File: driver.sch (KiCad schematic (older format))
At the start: 50 parts

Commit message: 5V raus
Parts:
- removed C?: 10u0, symbol Device:C
- removed C?: 10n0, symbol Device:C
- removed C?: 220u, symbol Device:C
- removed D?: B340, Diode_SMD:D_SMC, symbol Diode:B340
- removed L?: 15u0, symbol Device:L
- removed R?: 10k0, symbol Device:R
- removed R?: 3k24, symbol Device:R
- removed U?: TPS5430DDA, Package_SO:TI_SO-PowerPAD-8_ThermalVias, symbol Regulator_Switching:TPS5430DDA
- R?: value 3k24 -> 5k8
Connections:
- net labels removed: +5V
- wire segments 217 -> 190
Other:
- moved on the sheet: C?, D?, L?, R?, U?

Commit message: Power Supply geändert
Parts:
- removed C? (x2): 10u0, symbol Device:C
- removed C? (x2): 10n0, symbol Device:C
- removed C?: 220u, symbol Device:C
- removed C?: 10u0 / 75V, symbol Device:C
- removed C?: C, symbol Device:C
- removed C?: 10u0 / 16V, symbol Device:C
- removed C?: 100u, symbol Device:CP
- removed D?: B340, Diode_SMD:D_SMC, symbol Diode:B340
- removed L?: 15u0, symbol Device:L
- removed L?: L, symbol Device:L
- removed R? (x2): 10k0, symbol Device:R
- removed R?: 5k8, symbol Device:R
- removed R?: 402k, symbol Device:R
- removed R?: 2k00, symbol Device:R
- removed U?: TPS5430DDA, Package_SO:TI_SO-PowerPAD-8_ThermalVias, symbol Regulator_Switching:TPS5430DDA
- removed U?: LM5161, Package_SON:Texas_S-PVSON-N10_ThermalVias, symbol gsvesc:LM5161
- added C16: 10u/75V, symbol Device:C
- added C17, C19: 100n, symbol Device:C
- added C20, C23, C31: 10n0, symbol Device:C
- added C26: 22uF, symbol Device:C
- added C28: 10u0/25V, symbol Device:C
- added C33, C34: 100u, Capacitor_Tantalum_SMD:CP_EIA-3528-21_Kemet-B, symbol Device:CP
- added D4, D5: B360, Diode_SMD:D_SMC, symbol Diode:B360
- added L1: 470u, symbol Device:L
- added L2: 15u0, symbol Device:L
- added R12, R15: 680k, Resistor_SMD:R_0805_2012Metric, symbol Device:R
- added R16, R27: 10k0, Resistor_SMD:R_0805_2012Metric, symbol Device:R
- added R23: 2k70, Resistor_SMD:R_0805_2012Metric, symbol Device:R
- added R24: 1R00, Resistor_SMD:R_0805_2012Metric, symbol Device:R
- added R34: 5k90, Resistor_SMD:R_0805_2012Metric, symbol Device:R
- added U10: LM5008MM, Package_SO:MSOP-8_3x3mm_P0.65mm, symbol Regulator_Switching:LM5008MM
- added U14: TPS5430DDA, Package_SO:TI_SO-PowerPAD-8_ThermalVias, symbol Regulator_Switching:TPS5430DDA
- C15, C22, C29: renamed from C?; value 10u -> 10u0/25V; footprint (none) -> Capacitor_SMD:C_0805_2012Metric
- C18, C25, C30: renamed from C?; value C -> 100n; footprint (none) -> Capacitor_SMD:C_0805_2012Metric
- C21, C27, C32: renamed from C?; footprint (none) -> Capacitor_SMD:C_0805_2012Metric
- R13, R14, R17, R18, R19, R20, R21, R22: renamed from R?; footprint (none) -> Resistor_SMD:R_0805_2012Metric
- gave numbers to parts that had none: 6
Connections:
- net labels added: EXT_OFF
- wire segments 190 -> 191

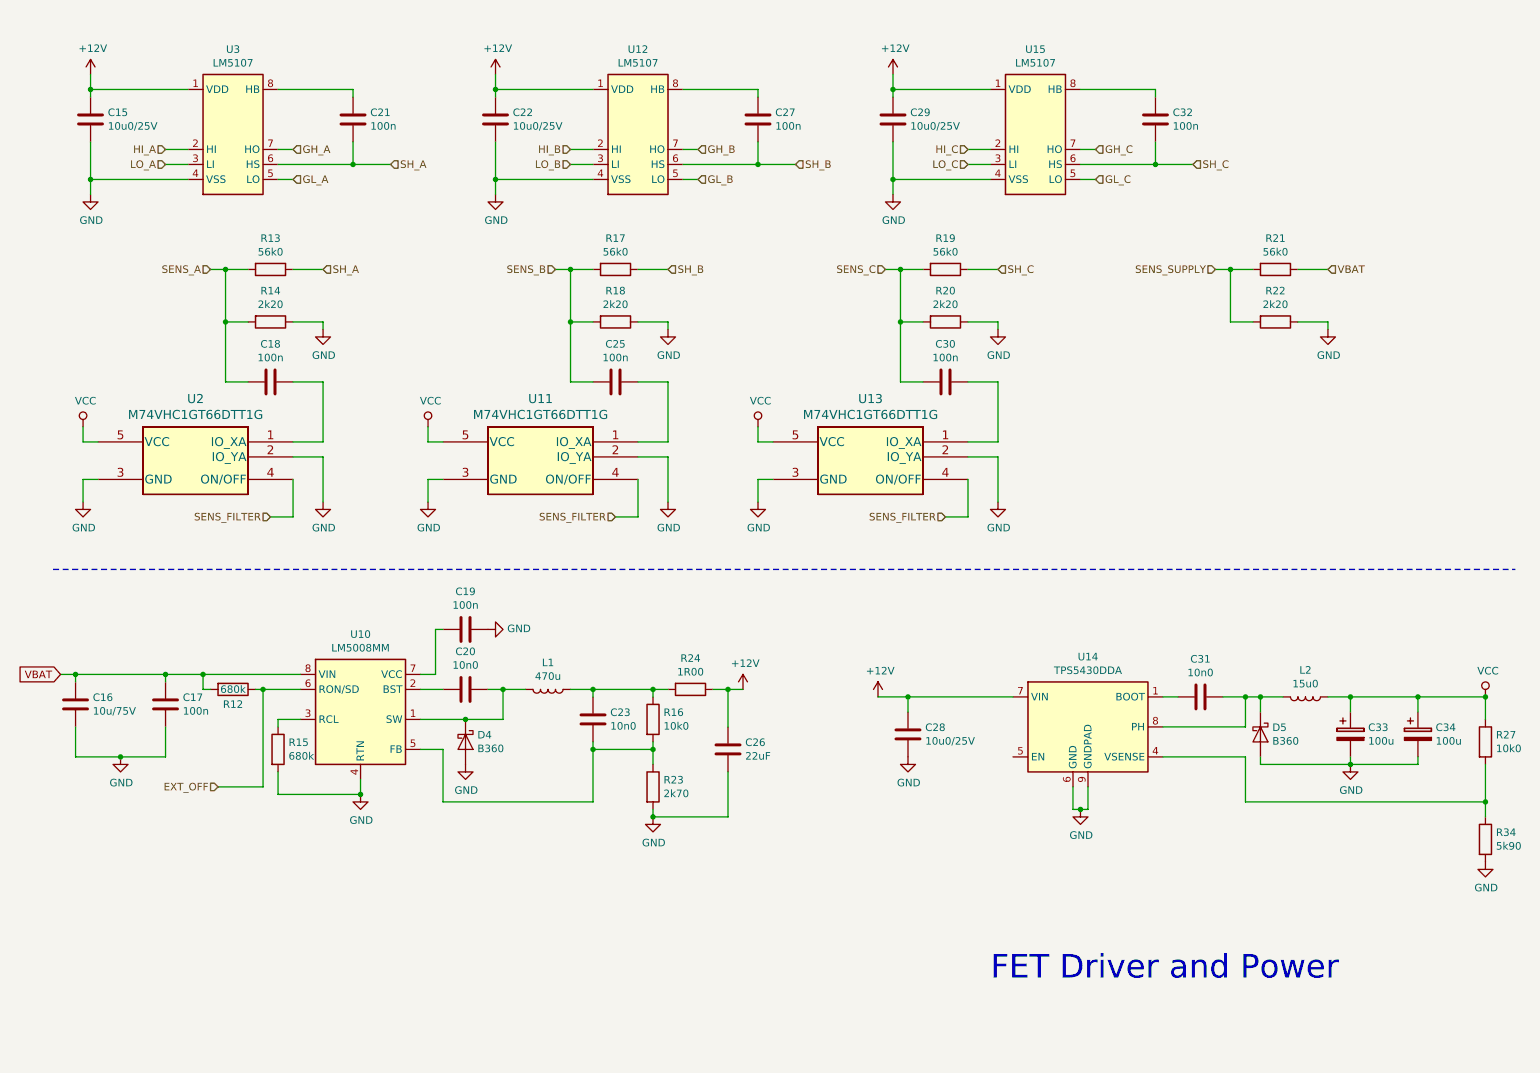
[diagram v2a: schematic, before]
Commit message: Powersupply geändert
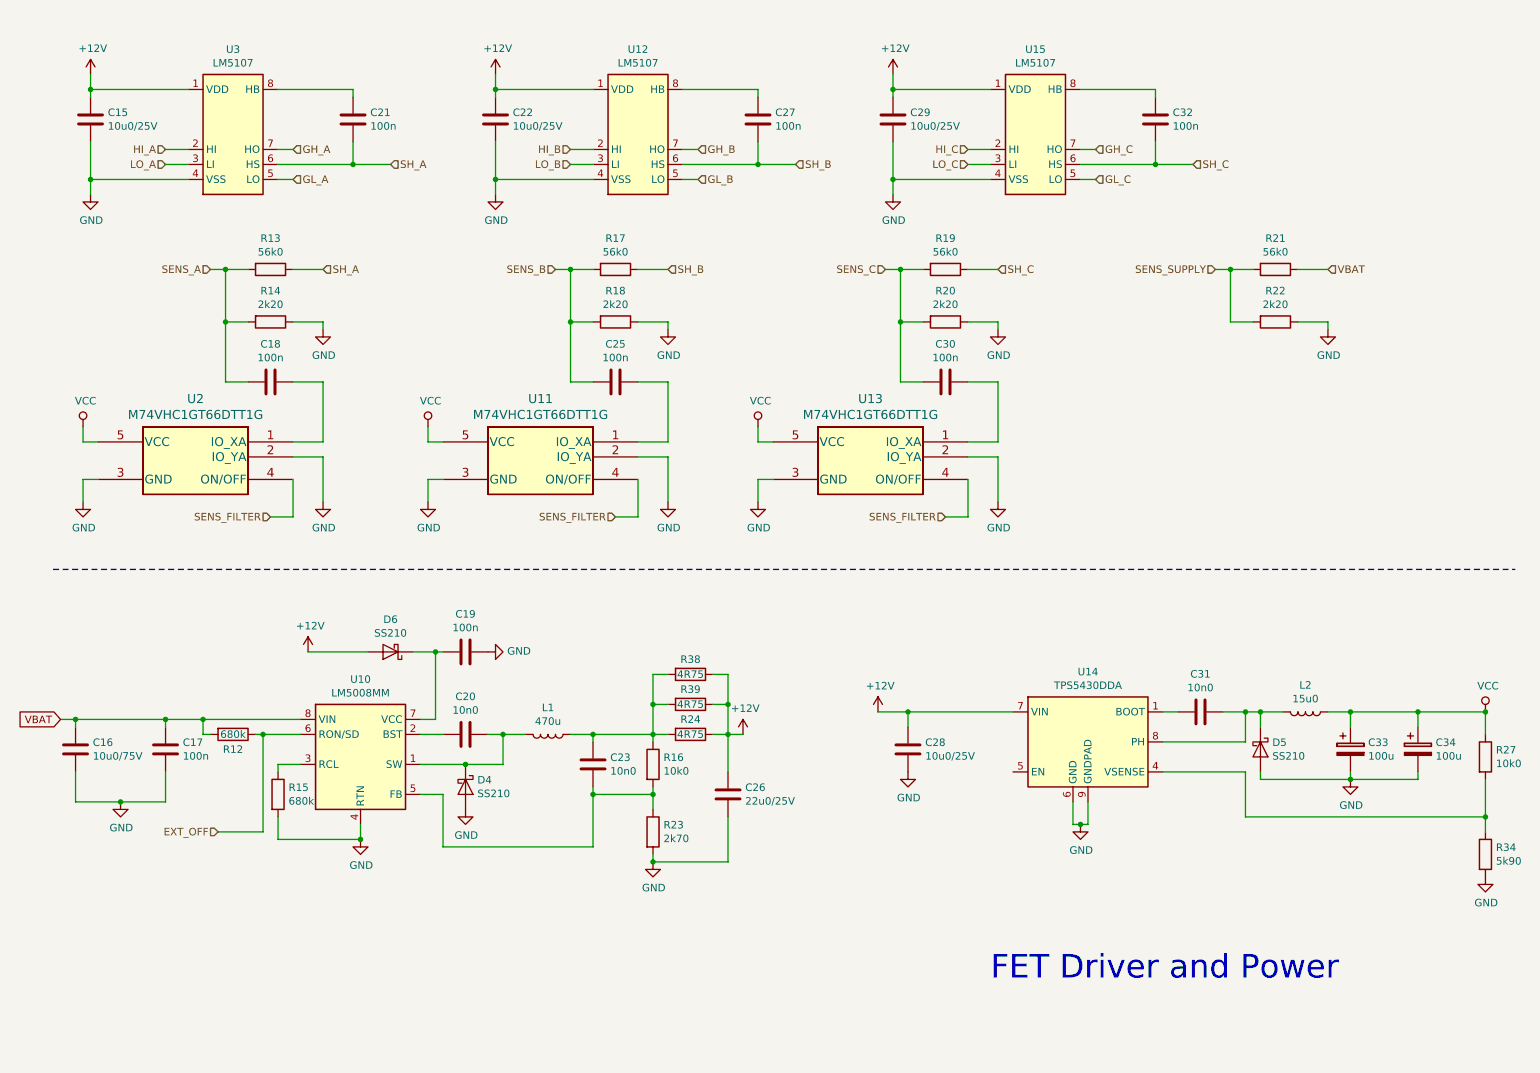
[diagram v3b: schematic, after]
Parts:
- added D6: SS210, Diode_SMD:D_SMA, symbol Device:D_Schottky
- added R38, R39: 4R75, Resistor_SMD:R_0805_2012Metric, symbol Device:R
- C16: value 10u/75V -> 10u0/75V; footprint (none) -> Capacitor_SMD:C_1210_3225Metric
- C17, C19, C20, C23, C28, C31: footprint (none) -> Capacitor_SMD:C_0805_2012Metric
- C26: value 22uF -> 22u0/25V; footprint (none) -> Capacitor_SMD:C_0805_2012Metric
- D4, D5: value B360 -> SS210; footprint Diode_SMD:D_SMC -> Diode_SMD:D_SMA; LCSC (none) -> C14996
- L1: footprint (none) -> Inductor_SMD:L_12x12mm_H6mm; LCSC (none) -> C169382; Partnumber (none) -> SWRB1207S-471MT
- L2: footprint (none) -> Inductor_SMD:L_12x12mm_H6mm; LCSC (none) -> C169384; Partnumber (none) -> SWRB1205S-150MT
- R24: value 1R00 -> 4R75
- U11, U13, U2: footprint TSOP-5 -> gsvesc:M74VHC1GT66DTT1G
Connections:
- net +12V: now also D6.2 (A), R38.1, R39.1
- net at C19.1, U10.7 (VCC): now also D6.1 (K)
- net at C23.1, L1.1, R16.1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: now also R38.2, R39.2
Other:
- moved on the sheet: C16, C17, C19, C20, C23, C26, C28, C31, C33, C34, D4, D5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

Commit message: V4 pre
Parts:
- added D7: B5819W, Diode_SMD:D_SOD-123, symbol Device:D_Schottky
- D6: value SS210 -> B5819W; footprint Diode_SMD:D_SMA -> Diode_SMD:D_SOD-123; LCSC C14996 -> C8598
- L2: footprint Inductor_SMD:L_12x12mm_H6mm -> Inductor_SMD:L_7.3x7.3_H4.5; LCSC C169384 -> C132136
- R14, R18, R20, R22: value 2k20 -> 2k70
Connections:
- net +12V: now also D7.1 (K)
- new net +5V: D7.2 (A)
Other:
- note added: "USB powered"
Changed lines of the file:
@@
 P 9050 2550
 F 0 "R22" V 8843 2550 50  0000 C CNN
-F 1 "2k20" V 8934 2550 50  0000 C CNN
+F 1 "2k70" V 8934 2550 50  0000 C CNN
 F 2 "Resistor_SMD:R_0805_2012Metric" V 8980 2550 50  0001 C CNN
 F 3 "~" H 9050 2550 50  0001 C CNN
@@
 P 6850 2550
 F 0 "R20" V 6643 2550 50  0000 C CNN
-F 1 "2k20" V 6734 2550 50  0000 C CNN
+F 1 "2k70" V 6734 2550 50  0000 C CNN
 F 2 "Resistor_SMD:R_0805_2012Metric" V 6780 2550 50  0001 C CNN
 F 3 "~" H 6850 2550 50  0001 C CNN
@@
 P 4650 2550
 F 0 "R18" V 4443 2550 50  0000 C CNN
-F 1 "2k20" V 4534 2550 50  0000 C CNN
+F 1 "2k70" V 4534 2550 50  0000 C CNN
 F 2 "Resistor_SMD:R_0805_2012Metric" V 4580 2550 50  0001 C CNN
 F 3 "~" H 4650 2550 50  0001 C CNN
@@
 P 2350 2550
 F 0 "R14" V 2143 2550 50  0000 C CNN
-F 1 "2k20" V 2234 2550 50  0000 C CNN
+F 1 "2k70" V 2234 2550 50  0000 C CNN
 F 2 "Resistor_SMD:R_0805_2012Metric" V 2280 2550 50  0001 C CNN
 F 3 "~" H 2350 2550 50  0001 C CNN
@@
 Wire Wire Line
 	4500 5700 4500 6050
-Wire Wire Line
-	7300 5150 6600 5150
 $Comp
 L power:+12V #PWR0147
@@
 F 0 "L2" V 9072 5150 50  0000 C CNN
 F 1 "15u0" V 9163 5150 50  0000 C CNN
-F 2 "Inductor_SMD:L_12x12mm_H6mm" H 9250 5150 50  0001 C CNN
+F 2 "Inductor_SMD:L_7.3x7.3_H4.5" H 9250 5150 50  0001 C CNN
 F 3 "~" H 9250 5150 50  0001 C CNN
 F 4 "SWRB1205S-150MT" V 9250 5150 50  0001 C CNN "Partnumber"
-F 5 "C169384" V 9250 5150 50  0001 C CNN "LCSC"
+F 5 "C132136" V 9250 5150 50  0001 C CNN "LCSC"
 	1    9250 5150
 	0    1    1    0
@@
 P 3150 4750
 F 0 "D6" H 3150 4534 50  0000 C CNN
-F 1 "SS210" H 3150 4625 50  0000 C CNN
-F 2 "Diode_SMD:D_SMA" H 3150 4750 50  0001 C CNN
+F 1 "B5819W" H 3150 4625 50  0000 C CNN
+F 2 "Diode_SMD:D_SOD-123" H 3150 4750 50  0001 C CNN
 F 3 "~" H 3150 4750 50  0001 C CNN
-F 4 "C14996" H 3150 4750 50  0001 C CNN "LCSC"
+F 4 "C8598" H 3150 4750 50  0001 C CNN "LCSC"
 	1    3150 4750
 	-1   0    0    1
@@
 	0    1    1    0
 $EndComp
+$Comp
+L Device:D_Schottky D7
+U 1 1 5E97305F
+P 7050 4900
+F 0 "D7" V 7100 4800 50  0000 C CNN
+F 1 "B5819W" V 7200 4700 50  0000 C CNN
+F 2 "Diode_SMD:D_SOD-123" H 7050 4900 50  0001 C CNN
+F 3 "~" H 7050 4900 50  0001 C CNN
+F 4 "C8598" H 7050 4900 50  0001 C CNN "LCSC"
+	1    7050 4900
+	0    -1   -1   0
+$EndComp
+Wire Wire Line
+	7050 4750 7050 4650
+Wire Wire Line
+	7050 4650 6400 4650
+$Comp
+L power:+5V #PWR0154
+U 1 1 5E97EB65
+P 6400 4650
+F 0 "#PWR0154" H 6400 4500 50  0001 C CNN
+F 1 "+5V" H 6415 4823 50  0000 C CNN
+F 2 "" H 6400 4650 50  0001 C CNN
+F 3 "" H 6400 4650 50  0001 C CNN
+	1    6400 4650
+	1    0    0    -1
+$EndComp
+Text Notes 6600 4550 0    79   ~ 0
+USB powered
+Wire Wire Line
+	6600 5150 7050 5150
+Wire Wire Line
+	7050 5050 7050 5150
+Connection ~ 7050 5150
+Wire Wire Line
+	7050 5150 7300 5150
 $EndSCHEMATC

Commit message: V4 alpha
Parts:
- U11, U13, U2: value M74VHC1GT66DTT1G -> SN74LVC1G66DBVR
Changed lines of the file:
@@
 P 5700 3550
 F 0 "U13" H 6350 4037 60  0000 C CNN
-F 1 "M74VHC1GT66DTT1G" H 6350 3931 60  0000 C CNN
+F 1 "SN74LVC1G66DBVR" H 6350 3931 60  0000 C CNN
 F 2 "gsvesc:M74VHC1GT66DTT1G" H 6200 3350 60  0001 C CNN
 F 3 "" H 5700 3550 60  0000 C CNN
@@
 P 3500 3550
 F 0 "U11" H 4150 4037 60  0000 C CNN
-F 1 "M74VHC1GT66DTT1G" H 4150 3931 60  0000 C CNN
+F 1 "SN74LVC1G66DBVR" H 4150 3931 60  0000 C CNN
 F 2 "gsvesc:M74VHC1GT66DTT1G" H 4000 3350 60  0001 C CNN
 F 3 "" H 3500 3550 60  0000 C CNN
@@
 P 1200 3550
 F 0 "U2" H 1850 4037 60  0000 C CNN
-F 1 "M74VHC1GT66DTT1G" H 1850 3931 60  0000 C CNN
+F 1 "SN74LVC1G66DBVR" H 1850 3931 60  0000 C CNN
 F 2 "gsvesc:M74VHC1GT66DTT1G" H 1700 3350 60  0001 C CNN
 F 3 "" H 1200 3550 60  0000 C CNN

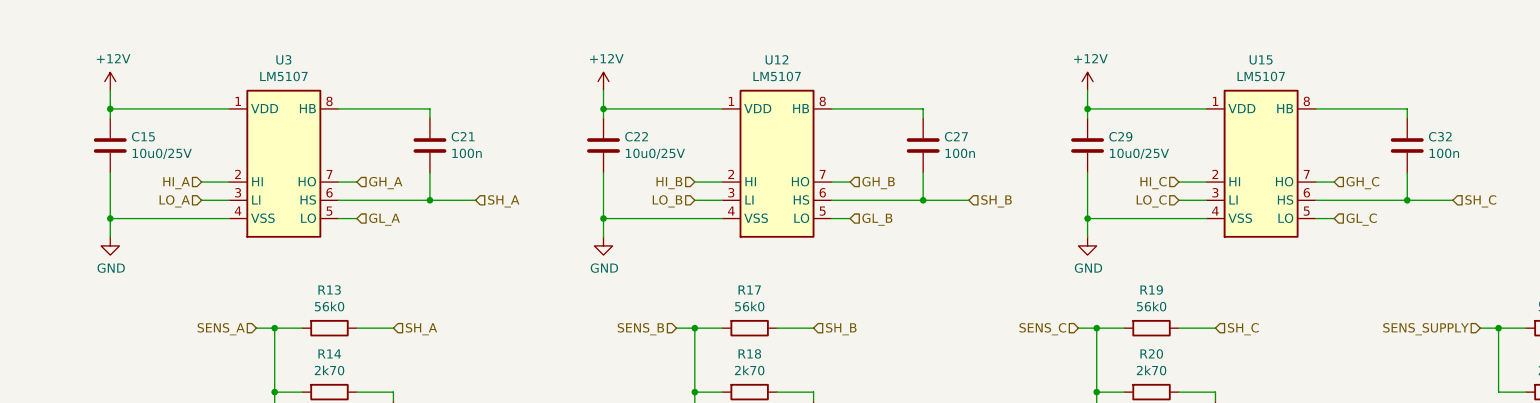
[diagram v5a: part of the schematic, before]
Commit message: Add boot-diode to use LM5109A as alternative FET driver
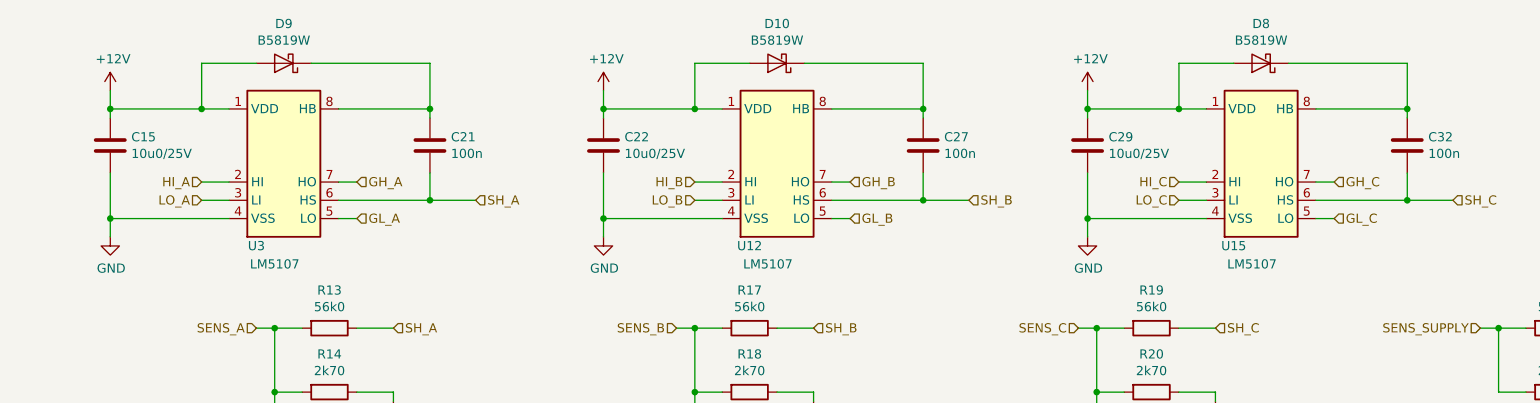
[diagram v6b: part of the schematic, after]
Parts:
- added D10, D8, D9: B5819W, Diode_SMD:D_SOD-123, symbol Device:D_Schottky
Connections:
- net +12V: now also D10.2 (A), D8.2 (A), D9.2 (A)
- net at C21.1, U3.8 (HB): now also D9.1 (K)
- net at C27.1, U12.8 (HB): now also D10.1 (K)
- net at C32.1, U15.8 (HB): now also D8.1 (K)
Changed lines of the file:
@@
 U 1 1 5E94B4D3
 P 2100 1300
-F 0 "U3" H 2100 1867 50  0000 C CNN
-F 1 "LM5107" H 2100 1776 50  0000 C CNN
+F 0 "U3" H 1950 850 50  0000 C CNN
+F 1 "LM5107" H 2050 750 50  0000 C CNN
 F 2 "Package_SO:SOIC-8_3.9x4.9mm_P1.27mm" H 2100 800 50  0001 C CIN
 F 3 "" H 2100 1300 50  0001 C CNN
@@
 LO_A
 Wire Wire Line
-	1800 1000 1150 1000
-Wire Wire Line
 	1800 1600 1150 1600
 $Comp
@@
 $EndComp
 Wire Wire Line
-	1150 1050 1150 1000
-Connection ~ 1150 1000
-Wire Wire Line
-	1150 1000 1150 900
-Wire Wire Line
 	1150 1350 1150 1600
 Connection ~ 1150 1600
@@
 U 1 1 5E94C6EA
 P 4800 1300
-F 0 "U12" H 4800 1867 50  0000 C CNN
-F 1 "LM5107" H 4800 1776 50  0000 C CNN
+F 0 "U12" H 4650 850 50  0000 C CNN
+F 1 "LM5107" H 4750 750 50  0000 C CNN
 F 2 "Package_SO:SOIC-8_3.9x4.9mm_P1.27mm" H 4800 800 50  0001 C CIN
 F 3 "" H 4800 1300 50  0001 C CNN
@@
 LO_B
 Wire Wire Line
-	4500 1000 3850 1000
-Wire Wire Line
 	4500 1600 3850 1600
 $Comp
@@
 U 1 1 5E94CC00
 P 7450 1300
-F 0 "U15" H 7450 1867 50  0000 C CNN
-F 1 "LM5107" H 7450 1776 50  0000 C CNN
+F 0 "U15" H 7300 850 50  0000 C CNN
+F 1 "LM5107" H 7400 750 50  0000 C CNN
 F 2 "Package_SO:SOIC-8_3.9x4.9mm_P1.27mm" H 7450 800 50  0001 C CIN
 F 3 "" H 7450 1300 50  0001 C CNN
@@
 Text HLabel 7000 1500 0    50   Input ~ 0
 LO_C
-Wire Wire Line
-	7150 1000 6500 1000
 Wire Wire Line
 	7150 1600 6500 1600
@@
 Wire Wire Line
 	7050 5150 7300 5150
+Connection ~ 1150 1000
+Wire Wire Line
+	1150 1000 1150 900
+Wire Wire Line
+	1150 1050 1150 1000
+Wire Wire Line
+	6500 1000 7000 1000
+$Comp
+L Device:D_Schottky D8
+U 1 1 5EA7F038
+P 7450 750
+F 0 "D8" H 7450 534 50  0000 C CNN
+F 1 "B5819W" H 7450 625 50  0000 C CNN
+F 2 "Diode_SMD:D_SOD-123" H 7450 750 50  0001 C CNN
+F 3 "~" H 7450 750 50  0001 C CNN
+F 4 "C8598" H 7450 750 50  0001 C CNN "LCSC"
+	1    7450 750
+	-1   0    0    1
+$EndComp
+Wire Wire Line
+	7000 1000 7000 750
+Wire Wire Line
+	7000 750  7300 750
+Wire Wire Line
+	8250 750  8250 1000
+Wire Wire Line
+	7600 750  8250 750
+Wire Wire Line
+	1150 1000 1650 1000
+Connection ~ 7000 1000
+Wire Wire Line
+	7000 1000 7150 1000
+Connection ~ 8250 1000
+Wire Wire Line
+	3850 1000 4350 1000
+$Comp
+L Device:D_Schottky D10
+U 1 1 5EABE0CB
+P 4800 750
+F 0 "D10" H 4800 534 50  0000 C CNN
+F 1 "B5819W" H 4800 625 50  0000 C CNN
+F 2 "Diode_SMD:D_SOD-123" H 4800 750 50  0001 C CNN
+F 3 "~" H 4800 750 50  0001 C CNN
+F 4 "C8598" H 4800 750 50  0001 C CNN "LCSC"
+	1    4800 750
+	-1   0    0    1
+$EndComp
+Wire Wire Line
+	4350 1000 4350 750
+Wire Wire Line
+	4350 750  4650 750
+Wire Wire Line
+	5600 750  5600 1000
+Wire Wire Line
+	4950 750  5600 750
+Connection ~ 4350 1000
+Wire Wire Line
+	4350 1000 4500 1000
+Connection ~ 5600 1000
+$Comp
+L Device:D_Schottky D9
+U 1 1 5EACAF3E
+P 2100 750
+F 0 "D9" H 2100 534 50  0000 C CNN
+F 1 "B5819W" H 2100 625 50  0000 C CNN
+F 2 "Diode_SMD:D_SOD-123" H 2100 750 50  0001 C CNN
+F 3 "~" H 2100 750 50  0001 C CNN
+F 4 "C8598" H 2100 750 50  0001 C CNN "LCSC"
+	1    2100 750
+	-1   0    0    1
+$EndComp
+Wire Wire Line
+	1650 1000 1650 750
+Wire Wire Line
+	1650 750  1950 750
+Wire Wire Line
+	2900 750  2900 1000
+Wire Wire Line
+	2250 750  2900 750
+Connection ~ 1650 1000
+Wire Wire Line
+	1650 1000 1800 1000
+Connection ~ 2900 1000
 $EndSCHEMATC

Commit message: einige Bauteile geändert, so dass sie Basic Parts bei JLC sind
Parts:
- D10, D8, D9: value B5819W -> SMMBD914LT3G; footprint Diode_SMD:D_SOD-123 -> Package_TO_SOT_SMD:SOT-23; symbol Device:D_Schottky -> Device:D
- R27: value 10k0 -> 13k0
- R34: value 5k90 -> 7k50
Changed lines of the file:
@@
 P 10450 5450
 F 0 "R27" H 10520 5496 50  0000 L CNN
-F 1 "10k0" H 10520 5405 50  0000 L CNN
+F 1 "13k0" H 10520 5405 50  0000 L CNN
 F 2 "Resistor_SMD:R_0805_2012Metric" V 10380 5450 50  0001 C CNN
 F 3 "~" H 10450 5450 50  0001 C CNN
@@
 P 10450 6100
 F 0 "R34" H 10520 6146 50  0000 L CNN
-F 1 "5k90" H 10520 6055 50  0000 L CNN
+F 1 "7k50" H 10520 6055 50  0000 L CNN
 F 2 "Resistor_SMD:R_0805_2012Metric" V 10380 6100 50  0001 C CNN
 F 3 "~" H 10450 6100 50  0001 C CNN
@@
 	6500 1000 7000 1000
 $Comp
-L Device:D_Schottky D8
+L Device:D D8
 U 1 1 5EA7F038
 P 7450 750
 F 0 "D8" H 7450 534 50  0000 C CNN
-F 1 "B5819W" H 7450 625 50  0000 C CNN
-F 2 "Diode_SMD:D_SOD-123" H 7450 750 50  0001 C CNN
+F 1 "SMMBD914LT3G" H 7450 625 50  0000 C CNN
+F 2 "Package_TO_SOT_SMD:SOT-23" H 7450 750 50  0001 C CNN
 F 3 "~" H 7450 750 50  0001 C CNN
 F 4 "C8598" H 7450 750 50  0001 C CNN "LCSC"
@@
 	3850 1000 4350 1000
 $Comp
-L Device:D_Schottky D10
+L Device:D D10
 U 1 1 5EABE0CB
 P 4800 750
 F 0 "D10" H 4800 534 50  0000 C CNN
-F 1 "B5819W" H 4800 625 50  0000 C CNN
-F 2 "Diode_SMD:D_SOD-123" H 4800 750 50  0001 C CNN
+F 1 "SMMBD914LT3G" H 4800 625 50  0000 C CNN
+F 2 "Package_TO_SOT_SMD:SOT-23" H 4800 750 50  0001 C CNN
 F 3 "~" H 4800 750 50  0001 C CNN
 F 4 "C8598" H 4800 750 50  0001 C CNN "LCSC"
@@
 Connection ~ 5600 1000
 $Comp
-L Device:D_Schottky D9
+L Device:D D9
 U 1 1 5EACAF3E
 P 2100 750
 F 0 "D9" H 2100 534 50  0000 C CNN
-F 1 "B5819W" H 2100 625 50  0000 C CNN
-F 2 "Diode_SMD:D_SOD-123" H 2100 750 50  0001 C CNN
+F 1 "SMMBD914LT3G" H 2100 625 50  0000 C CNN
+F 2 "Package_TO_SOT_SMD:SOT-23" H 2100 750 50  0001 C CNN
 F 3 "~" H 2100 750 50  0001 C CNN
 F 4 "C8598" H 2100 750 50  0001 C CNN "LCSC"
